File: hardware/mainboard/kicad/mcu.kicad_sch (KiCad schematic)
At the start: 12 parts, among them J15 J_STACK, U12 74HC138PW, U13 74HC4051PW

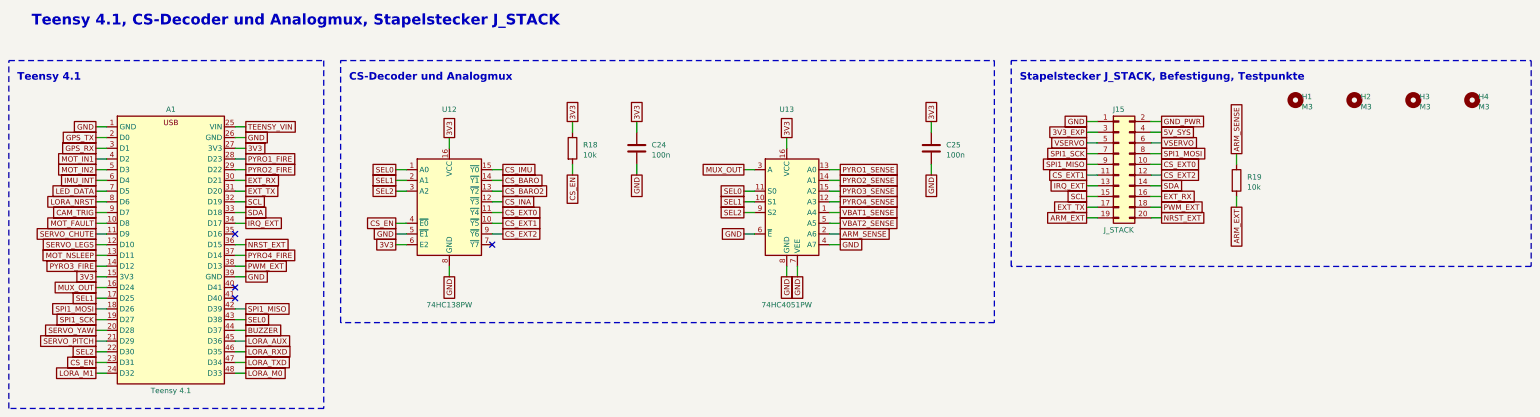
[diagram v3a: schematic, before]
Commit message: Platine rev B1: SPI0 auf J_STACK (E11), IMU LSM6DSV16X statt ICM-42688-P (E12), DRC 0/0
- J_STACK Pin 7/8/9 an SPI0 (Teensy 13/11/12) statt SPI1; nSLEEP -> 40, PYRO3_FIRE -> 41,
  PWM_EXT -> 33, LORA_M0 -> 16; keine Reservepins mehr (circuit.py, check_design.py, Doku)
- IMU LSM6DSV16X (C5267406) auf dem LGA-14-Footprint des ICM: Pins 2/3 an GND, 9-11 offen
  (AN5763 Tab. 1), JLC-Preis 3,4 statt 21,5 USD; Massepfad der IMU-Pads 2/3/6/7 ueber C26,
  3V3_SENS von Pad 5 ueber C26/C28 zu Pad 8
- die sieben neuen Wege von Hand geplant (eigene Sitzung 24.10.): 59 Vias, 13 kurze Stuecke
  auf B.Cu; SPI0_MISO 114 mm, SPI0-Takt zur Zusatzplatine hoechstens 8 MHz
- Reststummel (PYRO1_SENSE, PYRO4_SENSE, CS_IMU-Via, doppeltes GND-Via) entfernt
- sync_fields.py: Bauteilfelder der Platine aus circuit.py (Paritaet 0 ohne Neuerzeugung)
- DRC 0 Fehler, 0 offen, Paritaet 0; Pruefskript ohne Befund; Bestelldateien und Bilder neu
- Doku: Spezifikation, ORDER.md, Review-Brief, kicad-README (Par. 5.5 Tabelle der Wege, Par. 6
  E11/E12), Komponenten, Root-READMEs, PROJECT.md; HANDROUTING_SPI0.md

Co-Authored-By: Claude Fable 5.1 <noreply@anthropic.com>
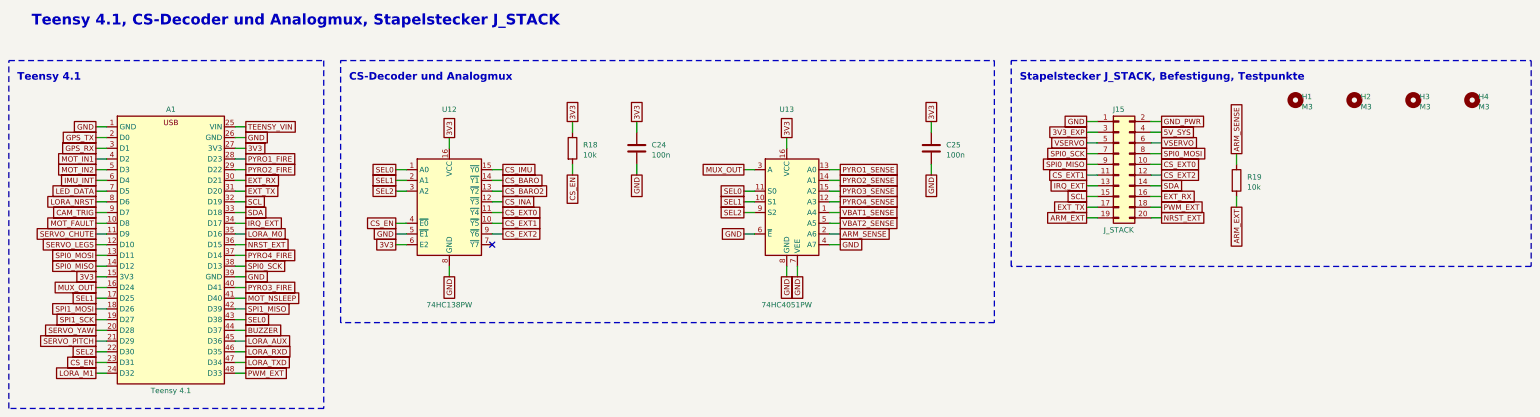
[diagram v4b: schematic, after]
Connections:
- net LORA_M0: now also A1.35 (D16); no longer A1.48 (D33)
- net MOT_NSLEEP: now also A1.41 (D40); no longer A1.13 (D11)
- net PWM_EXT: now also A1.48 (D33); no longer A1.38 (D13)
- net PYRO3_FIRE: now also A1.40 (D41); no longer A1.14 (D12)
- net SPI1_MISO: no longer J15.9 (Pin_9)
- net SPI1_MOSI: no longer J15.8 (Pin_8)
- net SPI1_SCK: no longer J15.7 (Pin_7)
- new net SPI0_MISO: A1.14 (D12), J15.9 (Pin_9)
- new net SPI0_MOSI: A1.13 (D11), J15.8 (Pin_8)
- new net SPI0_SCK: A1.38 (D13), J15.7 (Pin_7)
- no-connect marks 4 -> 1
